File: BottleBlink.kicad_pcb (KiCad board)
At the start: 2 copper layers, 70 x 70 mm, 61 parts, among them J1 Arduino_Nano_v2.x, J2 Conn_01x06_Male, U1 LM2904

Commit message: Add changes based on review comments
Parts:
- added JP1: NM, Resistor_SMD:R_0603_1608Metric_Pad0.98x0.95mm_HandSolder, F.Cu at (114.0, 103.8)
- added JP2: Jumper, Resistor_SMD:R_0603_1608Metric_Pad0.98x0.95mm_HandSolder, F.Cu at (115.9, 103.8)
- added R1: 10k, Resistor_SMD:R_0603_1608Metric_Pad0.98x0.95mm_HandSolder, F.Cu at (114.0, 99.7)
- added R6: 10k, Resistor_SMD:R_0603_1608Metric_Pad0.98x0.95mm_HandSolder, F.Cu at (115.9, 99.7)
- added SW1: SW_DPST_x2, Button_Switch_SMD:SW_SPST_EVQP0, B.Cu at (125.0, 95.0)
- added SW2: SW_DPST_x2, Button_Switch_SMD:SW_SPST_EVQP0, B.Cu at (125.0, 105.0)
- renumbered JP1 to JP3, JP2 to JP4, JP3 to JP5, R8 to R10, R9 to R11, R10 to R12, R11 to R13, R1 to R2, R2 to R3, R3 to R4, R4 to R5, R5 to R7, R6 to R8, R7 to R9
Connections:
- J1 pad 14: Net-(J1-Pad14) -> /Btn1
- J1 pad 15: Net-(J1-Pad15) -> /Btn2
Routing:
- net /Btn1: track 0.00 -> 27.3 mm, vias 0 -> 1
- net /Btn2: track 0.00 -> 24.6 mm, vias 0 -> 1
- net +3V3: track 65.9 -> 76.4 mm, vias 2 -> 3
- net Net-(JP1-Pad1): track 0.00 -> 6.07 mm
- net Net-(D11-Pad2): track 45.8 -> 42.5 mm
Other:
- board text added: "Skrooter Autdio BottleBlink V1.0.0 https://github.com/Skrooter/BottleBlink"
- board text added: "Up"
- board text removed: "Skrooter Autdio BottleBlink V1.0.0"

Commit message: Add LCSC numbers and QR code to PCB
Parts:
- added  : , BottleBlink:QrCode, B.Cu at (114.3, 119.4)
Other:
- board text added: "JLCJLCJLCJLC"

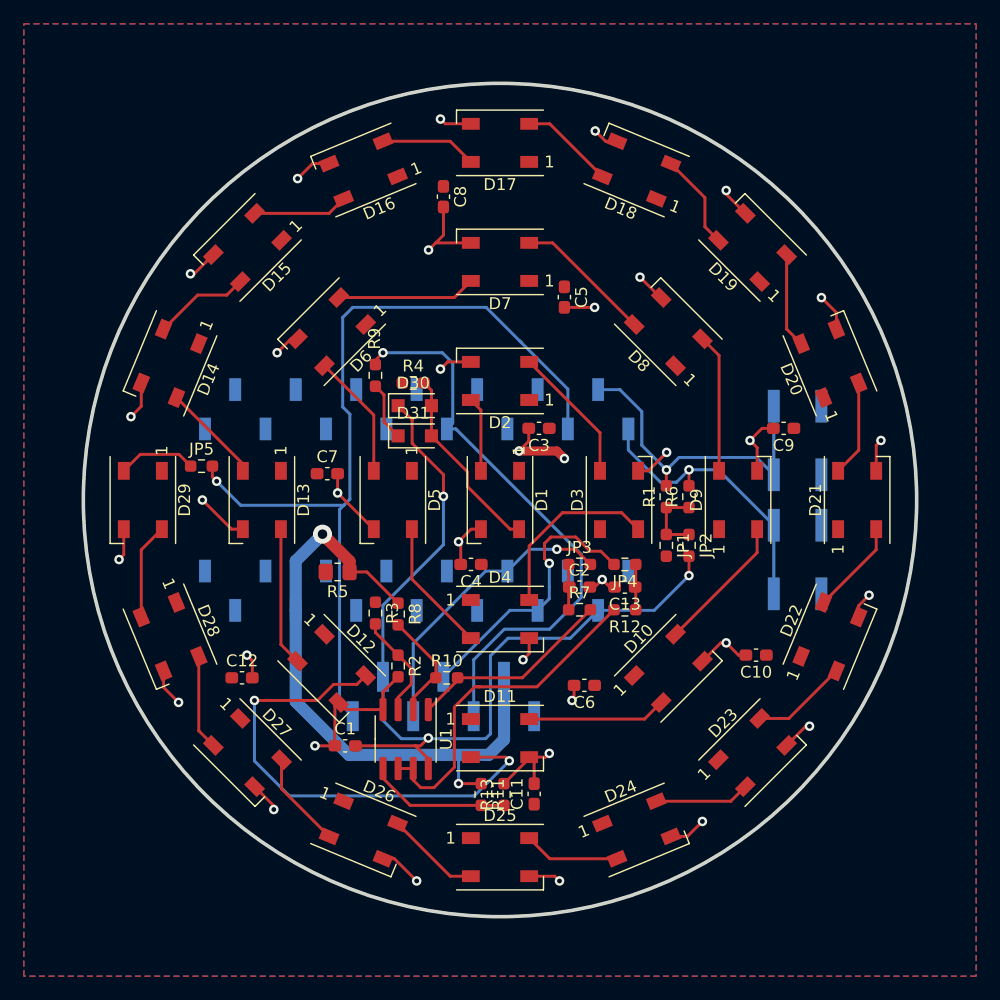
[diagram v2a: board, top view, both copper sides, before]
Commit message: Update to rev2
 * Removed a lot of components, e.g. current and voltage measurements
 * Added a 1u cap for each LED
 * Added more buttons
 * Updated silk
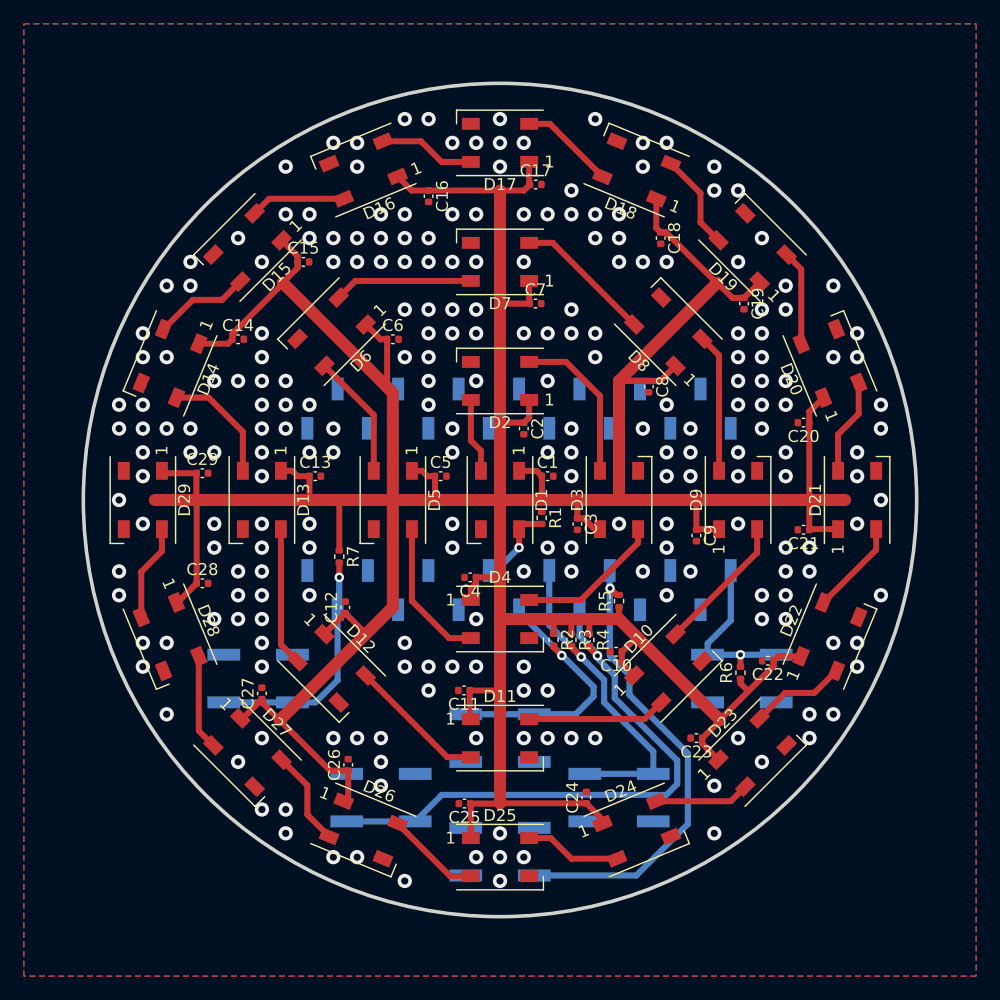
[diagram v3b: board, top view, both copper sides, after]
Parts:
- removed  : , BottleBlink:QrCode
- removed the C1 at (87.0, 120.7)
- removed the C2 at (106.7, 107.3)
- removed D30, D31: SM4007PL, Diode_SMD:D_SOD-123F
- removed J2: Conn_01x06_Male, Connector_PinHeader_2.54mm:PinHeader_1x07_P2.54mm_Vertical_SMD_Pin1Left
- removed JP1: NM, Resistor_SMD:R_0603_1608Metric_Pad0.98x0.95mm_HandSolder
- removed JP2, JP3, JP4, JP5: Jumper, Resistor_SMD:R_0603_1608Metric_Pad0.98x0.95mm_HandSolder
- removed R10: 220k, Resistor_SMD:R_0603_1608Metric_Pad0.98x0.95mm_HandSolder
- removed R11, R13: 10k, Resistor_SMD:R_0603_1608Metric_Pad0.98x0.95mm_HandSolder
- removed R12: 1k, Resistor_SMD:R_0603_1608Metric_Pad0.98x0.95mm_HandSolder
- removed the R2 at (91.4, 113.9)
- removed the R3 at (89.5, 109.5)
- removed R8: 1.8k, Resistor_SMD:R_0603_1608Metric_Pad0.98x0.95mm_HandSolder
- removed R9: 22, Resistor_SMD:R_0603_1608Metric_Pad0.98x0.95mm_HandSolder
- removed U1: LM2904, Package_SO:SOIC-8_3.9x4.9mm_P1.27mm
- added C11: 1u, Capacitor_SMD:C_0402_1005Metric, F.Cu at (97.0, 116.0)
- added C12: 1u, Capacitor_SMD:C_0402_1005Metric, F.Cu at (87.0, 109.0)
- added C14: 1u, Capacitor_SMD:C_0402_1005Metric, F.Cu at (78.0, 86.5)
- added C15: 1u, Capacitor_SMD:C_0402_1005Metric, F.Cu at (83.5, 80.0)
- added C16: 1u, Capacitor_SMD:C_0402_1005Metric, F.Cu at (94.0, 74.5)
- added C17: 1u, Capacitor_SMD:C_0402_1005Metric, F.Cu at (103.0, 73.5)
- added C18: 1u, Capacitor_SMD:C_0402_1005Metric, F.Cu at (113.5, 78.0)
- added C19: 1u, Capacitor_SMD:C_0402_1005Metric, F.Cu at (120.5, 83.5)
- added C20: 1u, Capacitor_SMD:C_0402_1005Metric, F.Cu at (125.5, 93.5)
- added C21: 1u, Capacitor_SMD:C_0402_1005Metric, F.Cu at (125.5, 102.5)
- added C22: 1u, Capacitor_SMD:C_0402_1005Metric, F.Cu at (122.5, 113.5)
- added C23: 1u, Capacitor_SMD:C_0402_1005Metric, F.Cu at (116.5, 120.0)
- added C24: 1u, Capacitor_SMD:C_0402_1005Metric, F.Cu at (107.2, 125.0)
- added C25: 1u, Capacitor_SMD:C_0402_1005Metric, F.Cu at (97.0, 125.5)
- added C26: 1u, Capacitor_SMD:C_0402_1005Metric, F.Cu at (87.2, 122.2)
- added C27: 1u, Capacitor_SMD:C_0402_1005Metric, F.Cu at (80.0, 116.2)
- added C28: 1u, Capacitor_SMD:C_0402_1005Metric, F.Cu at (75.0, 107.0)
- added C29: 1u, Capacitor_SMD:C_0402_1005Metric, F.Cu at (75.0, 97.8)
- added R1: 1k, Resistor_SMD:R_0402_1005Metric, F.Cu at (103.5, 101.5)
- added R6: 10k, Resistor_SMD:R_0402_1005Metric, F.Cu at (120.2, 114.5)
- added SW3: SW_DPST_x2, Button_Switch_SMD:SW_SPST_EVQP0, B.Cu at (90.0, 125.0)
- added SW4: SW_DPST_x2, Button_Switch_SMD:SW_SPST_EVQP0, B.Cu at (100.0, 129.5)
- added SW5: SW_DPST_x2, Button_Switch_SMD:SW_SPST_EVQP0, B.Cu at (120.3, 115.0)
- added SW6: SW_DPST_x2, Button_Switch_SMD:SW_SPST_EVQP0, B.Cu at (79.7, 115.0)
- C1: renamed from C3; footprint Capacitor_SMD:C_0603_1608Metric_Pad1.08x0.95mm_HandSolder -> Capacitor_SMD:C_0402_1005Metric
- C10: renamed from C12; footprint Capacitor_SMD:C_0603_1608Metric_Pad1.08x0.95mm_HandSolder -> Capacitor_SMD:C_0402_1005Metric
- C13: value 10n -> 1u; footprint Capacitor_SMD:C_0603_1608Metric_Pad1.08x0.95mm_HandSolder -> Capacitor_SMD:C_0402_1005Metric
- C2: renamed from C4; footprint Capacitor_SMD:C_0603_1608Metric_Pad1.08x0.95mm_HandSolder -> Capacitor_SMD:C_0402_1005Metric
- C3: renamed from C5; footprint Capacitor_SMD:C_0603_1608Metric_Pad1.08x0.95mm_HandSolder -> Capacitor_SMD:C_0402_1005Metric
- C4: renamed from C6; footprint Capacitor_SMD:C_0603_1608Metric_Pad1.08x0.95mm_HandSolder -> Capacitor_SMD:C_0402_1005Metric
- C5: renamed from C7; footprint Capacitor_SMD:C_0603_1608Metric_Pad1.08x0.95mm_HandSolder -> Capacitor_SMD:C_0402_1005Metric
- C6: renamed from C8; footprint Capacitor_SMD:C_0603_1608Metric_Pad1.08x0.95mm_HandSolder -> Capacitor_SMD:C_0402_1005Metric
- C7: renamed from C9; footprint Capacitor_SMD:C_0603_1608Metric_Pad1.08x0.95mm_HandSolder -> Capacitor_SMD:C_0402_1005Metric
- C8: renamed from C10; footprint Capacitor_SMD:C_0603_1608Metric_Pad1.08x0.95mm_HandSolder -> Capacitor_SMD:C_0402_1005Metric
- C9: renamed from C11; footprint Capacitor_SMD:C_0603_1608Metric_Pad1.08x0.95mm_HandSolder -> Capacitor_SMD:C_0402_1005Metric
- J1: footprint BottleBlink:ArduinoNanoSMD -> SkrooterFootprints:ArduinoNanoSMD
- R2: renamed from R1; footprint Resistor_SMD:R_0603_1608Metric_Pad0.98x0.95mm_HandSolder -> Resistor_SMD:R_0402_1005Metric
- R3: renamed from R6; footprint Resistor_SMD:R_0603_1608Metric_Pad0.98x0.95mm_HandSolder -> Resistor_SMD:R_0402_1005Metric
- R4, R7: value 1k -> 10k; footprint Resistor_SMD:R_0603_1608Metric_Pad0.98x0.95mm_HandSolder -> Resistor_SMD:R_0402_1005Metric
- R5: value 10m -> 10k; footprint Resistor_SMD:R_0805_2012Metric_Pad1.20x1.40mm_HandSolder -> Resistor_SMD:R_0402_1005Metric
- moved SW1 35.4 mm to (100.0, 120.0), turned to 0 degrees
- moved C10 31.5 mm to (109.8, 112.8), turned to 180 degrees
- moved C13 27.6 mm to (84.5, 98.0), turned to 0 degrees
- moved R4 26.2 mm to (107.5, 111.8), turned to -90 degrees
- moved C9 25.6 mm to (116.5, 103.0), turned to -90 degrees
- moved SW2 25.0 mm to (110.0, 125.0), turned to 0 degrees
- moved C8 24.3 mm to (112.5, 90.5), turned to -90 degrees
- moved R5 23.8 mm to (110.0, 108.5), turned to 90 degrees
- moved C7 23.3 mm to (103.0, 83.5), turned to 0 degrees
- moved R7 20.7 mm to (86.5, 104.8), turned to -90 degrees
- moved C3 19.1 mm to (106.5, 102.0)
- moved R3 15.6 mm to (106.0, 111.8), turned to -90 degrees
- moved R2 15.3 mm to (104.5, 111.7), turned to -90 degrees
- moved C4 13.2 mm to (97.5, 106.5)
- moved C6 12.7 mm to (91.0, 86.5), turned to 0 degrees
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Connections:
- C1 pad 1: +5VL -> +5V
- C10 pad 1: +5VL -> +5V
- C13 pad 1: Net-(C13-Pad1) -> +5V
- C2 pad 1: +5VL -> +5V
- C3 pad 1: +5VL -> +5V
- C4 pad 1: +5VL -> +5V
- C5 pad 1: +5VL -> +5V
- C6 pad 1: +5VL -> +5V
- C7 pad 1: +5VL -> +5V
- C8 pad 1: +5VL -> +5V
- C9 pad 1: +5VL -> +5V
- D1 pad 1: +5VL -> +5V
- D10 pad 1: +5VL -> +5V
- D11 pad 1: +5VL -> +5V
- D12 pad 1: +5VL -> +5V
- D13 pad 1: +5VL -> +5V
- D14 pad 1: +5VL -> +5V
- D15 pad 1: +5VL -> +5V
- D16 pad 1: +5VL -> +5V
- D17 pad 1: +5VL -> +5V
- D18 pad 1: +5VL -> +5V
- D19 pad 1: +5VL -> +5V
- D2 pad 1: +5VL -> +5V
- D20 pad 1: +5VL -> +5V
- D21 pad 1: +5VL -> +5V
- D22 pad 1: +5VL -> +5V
- D23 pad 1: +5VL -> +5V
- D24 pad 1: +5VL -> +5V
- D25 pad 1: +5VL -> +5V
- D26 pad 1: +5VL -> +5V
- D27 pad 1: +5VL -> +5V
- D28 pad 1: +5VL -> +5V
- D29 pad 1: +5VL -> +5V
- D29 pad 2: /LedOut -> unconnected-(D29-DOUT-Pad2)
- D3 pad 1: +5VL -> +5V
- D4 pad 1: +5VL -> +5V
- D5 pad 1: +5VL -> +5V
- D6 pad 1: +5VL -> +5V
- D7 pad 1: +5VL -> +5V
- D8 pad 1: +5VL -> +5V
- D9 pad 1: +5VL -> +5V
- J1 pad 1: Net-(J1-Pad1) -> /Btn5
- J1 pad 10: Net-(J1-Pad10) -> unconnected-(J1-D7-Pad10)
- J1 pad 11: Net-(J1-Pad11) -> unconnected-(J1-D8-Pad11)
- J1 pad 12: Net-(J1-Pad12) -> unconnected-(J1-D9-Pad12)
- J1 pad 13: Net-(J1-Pad13) -> unconnected-(J1-D10-Pad13)
- J1 pad 14: /Btn1 -> /Btn6
- J1 pad 15: /Btn2 -> unconnected-(J1-D12-Pad15)
- J1 pad 16: Net-(J1-Pad16) -> unconnected-(J1-D13-Pad16)
- J1 pad 18: Net-(J1-Pad18) -> unconnected-(J1-AREF-Pad18)
- J1 pad 19: /Adc5V -> unconnected-(J1-A0-Pad19)
- J1 pad 2: Net-(J1-Pad2) -> unconnected-(J1-D0/RX-Pad2)
- J1 pad 20: /AdcShunt -> unconnected-(J1-A1-Pad20)
- J1 pad 21: Net-(J1-Pad21) -> unconnected-(J1-A2-Pad21)
- J1 pad 22: Net-(J1-Pad22) -> unconnected-(J1-A3-Pad22)
- J1 pad 23: Net-(J1-Pad23) -> unconnected-(J1-A4-Pad23)
- J1 pad 24: Net-(J1-Pad24) -> unconnected-(J1-A5-Pad24)
- J1 pad 25: Net-(J1-Pad25) -> unconnected-(J1-A6-Pad25)
- J1 pad 26: Net-(J1-Pad26) -> unconnected-(J1-A7-Pad26)
- J1 pad 28: Net-(J1-Pad28) -> unconnected-(J1-~{RESET}-Pad28)
- J1 pad 3: Net-(J1-Pad3) -> unconnected-(J1-~{RESET}-Pad3)
- J1 pad 30: Net-(J1-Pad30) -> unconnected-(J1-VIN-Pad30)
- J1 pad 5: Net-(J1-Pad5) -> /Btn4
- J1 pad 6: Net-(J1-Pad6) -> /Btn3
- J1 pad 7: Net-(J1-Pad7) -> /Btn2
- J1 pad 8: Net-(J1-Pad8) -> /Btn1
- J1 pad 9: /LedIn3v -> /LedIn
- R2 pad 1: Net-(JP1-Pad1) -> +5V
- R3 pad 1: Net-(JP1-Pad1) -> +5V
- R4 pad 1: +5VL -> +5V
- R4 pad 2: /LedIn -> /Btn3
- R5 pad 2: +5VL -> /Btn4
- R7 pad 1: Net-(C2-Pad1) -> +5V
- R7 pad 2: Net-(R10-Pad2) -> /Btn6
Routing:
- net +5V: track 54.0 -> 383.1 mm, vias 2 -> 0
- net GND: track 124.3 -> 0.00 mm, vias 35 -> 235
- net +3V3: track 76.4 -> 0.00 mm, vias 3 -> 0
- net Net-(J1-Pad13): track 73.2 -> 0.00 mm, vias 1 -> 0
- net /LedIn3v: track 48.4 -> 0.00 mm, vias 1 -> 0
- net /Btn3: track 0.00 -> 48.2 mm, vias 0 -> 1
- net /Btn4: track 0.00 -> 39.7 mm, vias 0 -> 1
- net Net-(D11-DOUT): track 42.5 -> 11.7 mm, vias 2 -> 0
- net Net-(R12-Pad2): track 28.7 -> 0.00 mm
- net /AdcShunt: track 25.2 -> 0.00 mm, vias 1 -> 0
- net /Adc5V: track 23.4 -> 0.00 mm, vias 1 -> 0
- net /Btn6: track 0.00 -> 20.3 mm, vias 0 -> 1
- net Net-(R10-Pad2): track 17.2 -> 0.00 mm
- net /Btn5: track 0.00 -> 14.6 mm, vias 0 -> 1
- net Net-(R11-Pad2): track 11.9 -> 0.00 mm
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- added copper zone on F.Cu, net GND
- removed copper zone on F.Cu, net +5VL
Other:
- net class Default removed
- board text added: "Skrooter Autdio BottleBlink V2.0.0 https://github.com/Skrooter/BottleBlink"
- board text removed: "Skrooter Autdio BottleBlink V1.0.0 https://github.com/Skrooter/BottleBlink"

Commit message: Final fixes before production
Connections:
- J1 pad 17: +3V3 -> unconnected-(J1-3V3-Pad17)
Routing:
- net /Btn4: track 39.7 -> 46.9 mm
- net +5V: track 383.1 -> 379.5 mm, vias 0 -> 1
